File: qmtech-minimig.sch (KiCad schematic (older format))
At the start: 0 parts

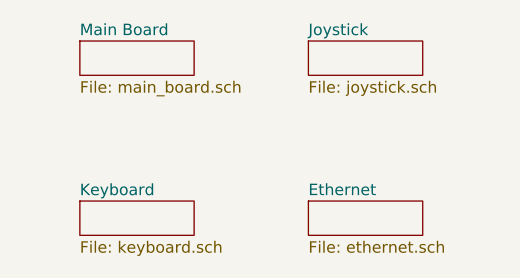
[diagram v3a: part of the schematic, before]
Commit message: First step to implement floppy interface. ESP32 check wireing in.
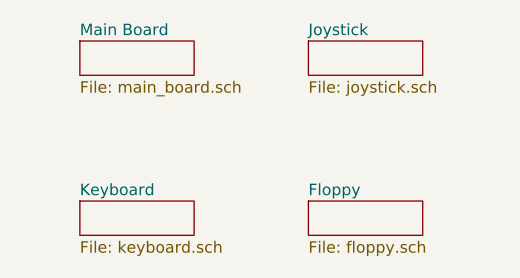
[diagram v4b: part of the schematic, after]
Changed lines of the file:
@@
 S 5500 2200 500  150
 U 5DE41876
-F0 "Ethernet" 50
-F1 "ethernet.sch" 50
+F0 "Floppy" 50
+F1 "floppy.sch" 50
 $EndSheet
 $EndSCHEMATC

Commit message: First checkin of SDRAM Open AARS board.
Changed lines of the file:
@@
 $Descr A4 11693 8268
 encoding utf-8
-Sheet 1 9
+Sheet 1 10
 Title ""
 Date ""
@@
 F1 "floppy.sch" 50
 $EndSheet
+$Sheet
+S 2075 2900 500  150
+U 5F1B034D
+F0 "SDRAM" 50
+F1 "sdram.sch" 50
+$EndSheet
 $EndSCHEMATC

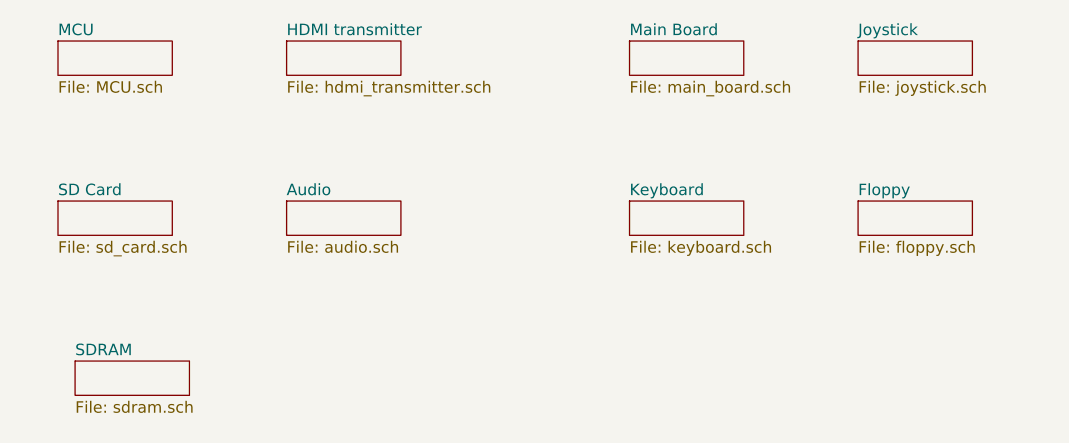
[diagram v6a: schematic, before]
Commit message: Remove kicad 5 files, add kicad 6 files.
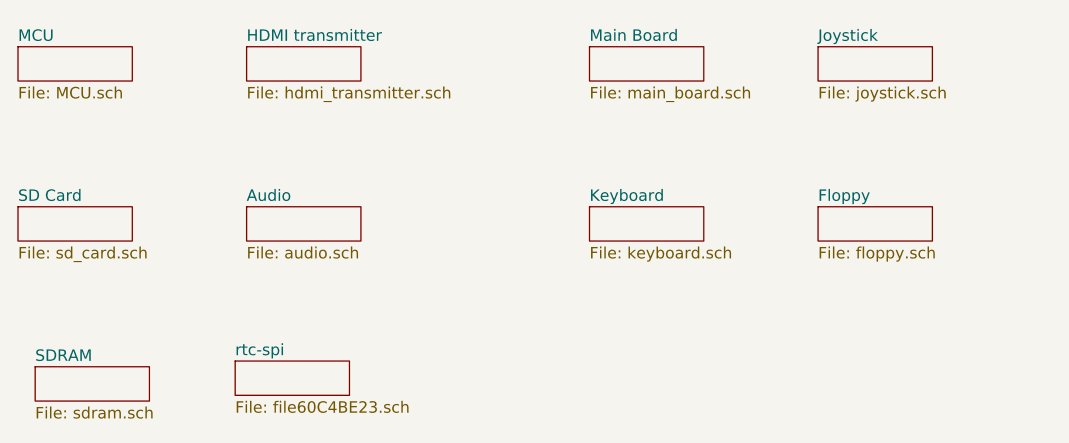
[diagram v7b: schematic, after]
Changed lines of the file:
@@
 $Descr A4 11693 8268
 encoding utf-8
-Sheet 1 10
+Sheet 1 11
 Title ""
 Date ""
@@
 $EndDescr
 $Sheet
-S 2000 1500 500  150
+S 1825 1525 500  150
 U 5D5D9AB7
 F0 "MCU" 50
@@
 $EndSheet
 $Sheet
-S 3000 1500 500  150
+S 2825 1525 500  150
 U 5D6A6E73
 F0 "HDMI transmitter" 50
@@
 $EndSheet
 $Sheet
-S 4500 1500 500  150
+S 4325 1525 500  150
 U 5D7064D1
 F0 "Main Board" 50
@@
 $EndSheet
 $Sheet
-S 5500 1500 500  150
+S 5325 1525 500  150
 U 5D74B9F4
 F0 "Joystick" 50
@@
 $EndSheet
 $Sheet
-S 2000 2200 500  150
+S 1825 2225 500  150
 U 5D7BA5F4
 F0 "SD Card" 50
@@
 $EndSheet
 $Sheet
-S 3000 2200 500  150
+S 2825 2225 500  150
 U 5DC624C0
 F0 "Audio" 50
@@
 $EndSheet
 $Sheet
-S 4500 2200 500  150
+S 4325 2225 500  150
 U 5DC624E5
 F0 "Keyboard" 50
@@
 $EndSheet
 $Sheet
-S 5500 2200 500  150
+S 5325 2225 500  150
 U 5DE41876
 F0 "Floppy" 50
@@
 $EndSheet
 $Sheet
-S 2075 2900 500  150
+S 1900 2925 500  150
 U 5F1B034D
 F0 "SDRAM" 50
 F1 "sdram.sch" 50
 $EndSheet
+$Sheet
+S 2775 2900 500  150
+U 60C4BE24
+F0 "rtc-spi" 50
+F1 "file60C4BE23.sch" 50
+$EndSheet
 $EndSCHEMATC
